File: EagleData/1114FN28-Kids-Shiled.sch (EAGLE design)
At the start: 18 parts

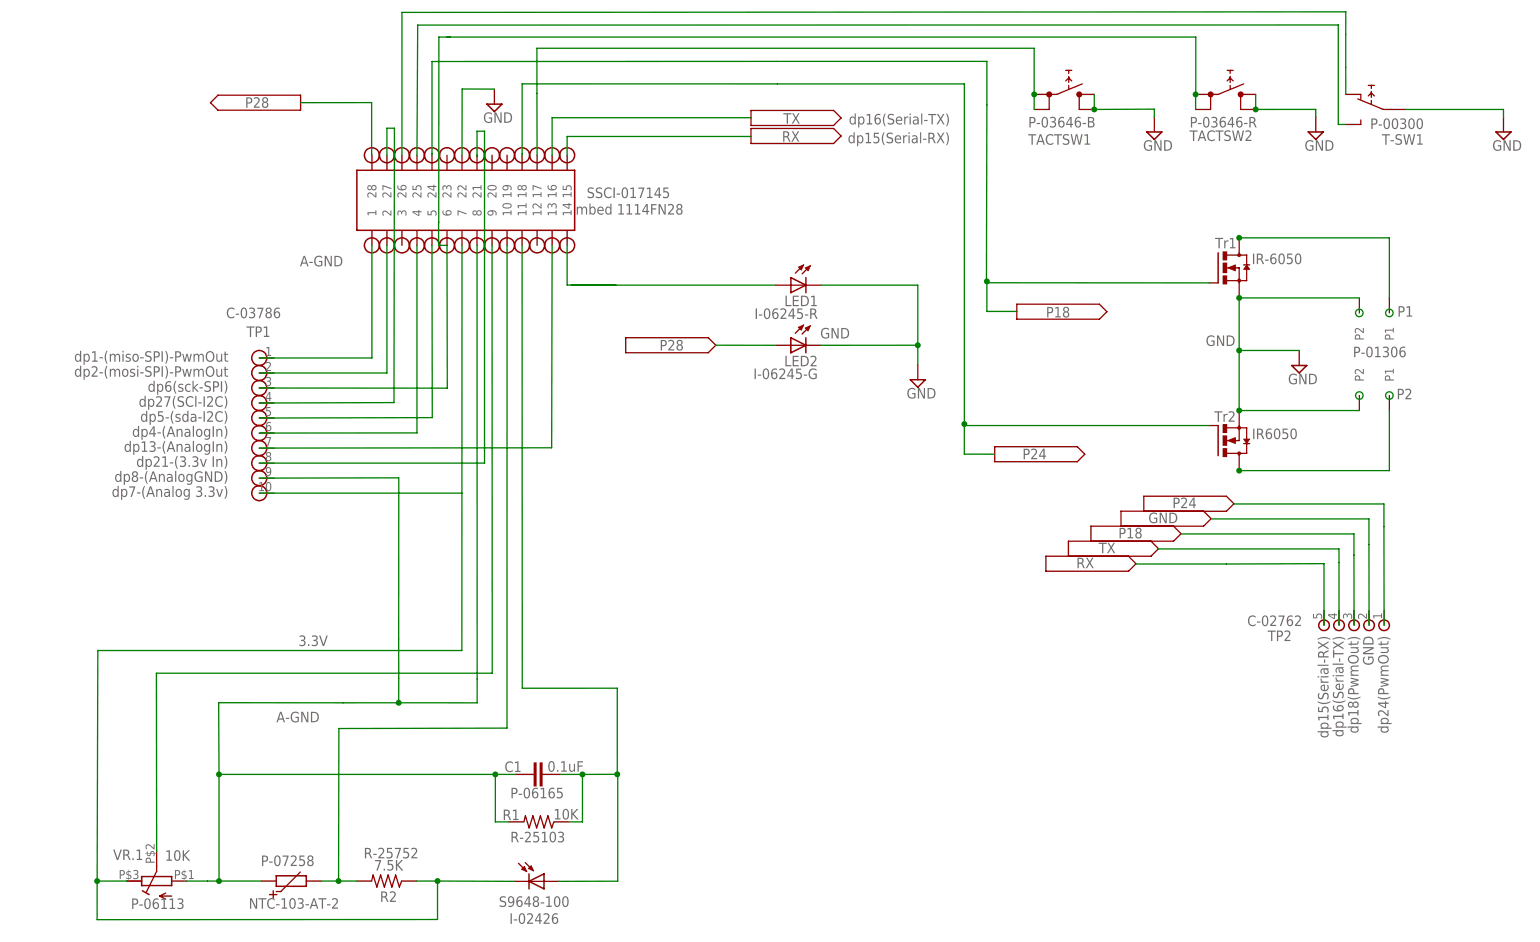
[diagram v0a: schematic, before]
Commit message: Change to FET part number.
I-6050 to I-6025 AKIZUKI part number.
IRLU3410PBF
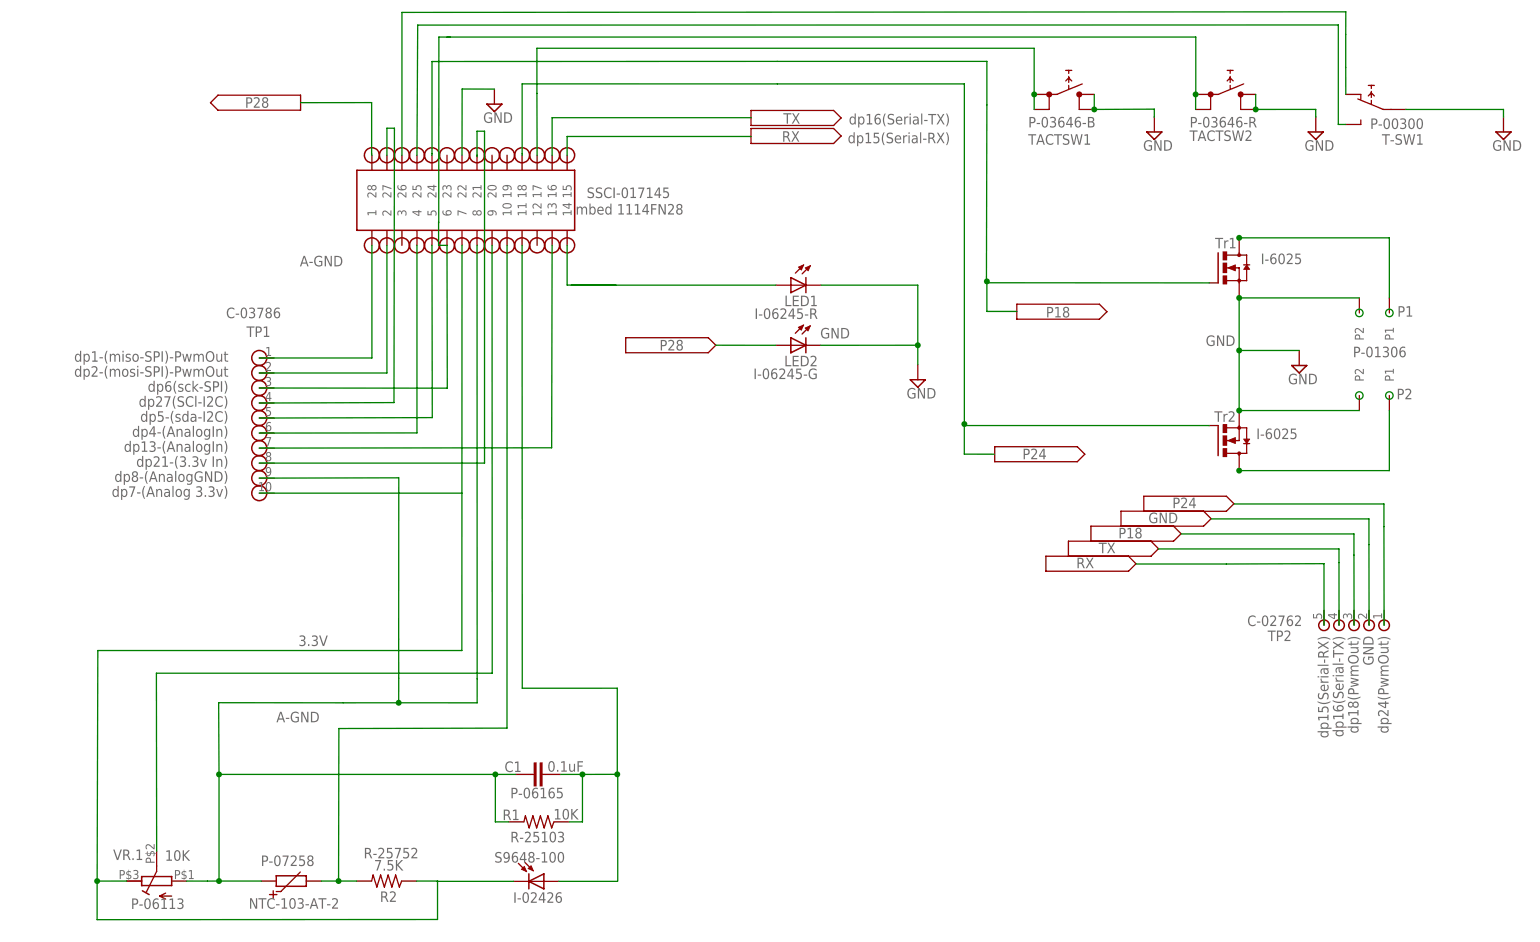
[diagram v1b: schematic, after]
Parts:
- U$2: device Aruduino-Kids-Shiled:S9648-100 -> 1114FN28-Kids-Shiled:S9648-100
- U$4: value IR-6050 -> I-6025
- U$5: value IR6050 -> I-6025
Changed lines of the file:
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@@
 <setting verticaltext="up"/>
 </settings>
-<grid distance="50" unitdist="mil" unit="mil" style="lines" multiple="1" display="yes" altdistance="5" altunitdist="mil" altunit="mil"/>
+<grid distance="5" unitdist="mil" unit="mil" style="lines" multiple="1" display="no" altdistance="5" altunitdist="mil" altunit="mil"/>
 <layers>
 <layer number="1" name="Top" color="4" fill="1" visible="no" active="no"/>
@@
 <part name="TB2" library="Aruduino-Kids-Shiled" deviceset="TB112-2-2-U-1" device="" value="P-01306"/>
 <part name="VR.1" library="Aruduino-Kids-Shiled" deviceset="TSR-3386K" device="" value="10K"/>
-<part name="U$4" library="Aruduino-Kids-Shiled" deviceset="ＩＲＦＵ１２０Ｎ" device="" value="IR-6050"/>
-<part name="U$5" library="Aruduino-Kids-Shiled" deviceset="ＩＲＦＵ１２０Ｎ" device="" value="IR6050"/>
+<part name="U$4" library="Aruduino-Kids-Shiled" deviceset="ＩＲＦＵ１２０Ｎ" device="" value="I-6025"/>
+<part name="U$5" library="Aruduino-Kids-Shiled" deviceset="ＩＲＦＵ１２０Ｎ" device="" value="I-6025"/>
 <part name="U$1" library="Aruduino-Kids-Shiled" deviceset="FH-1X14" device=""/>
-<part name="U$2" library="Aruduino-Kids-Shiled" deviceset="S9648-100" device=""/>
 <part name="C1" library="Aruduino-Kids-Shiled" deviceset="C-RPEF" device="" value="0.1uF"/>
 <part name="R1" library="Aruduino-Kids-Shiled" deviceset="R" device="" value="10K"/>
@@
 <part name="SUPPLY16" library="supply2" deviceset="V&lt;--" device="" value=""/>
 <part name="SUPPLY17" library="supply2" deviceset="V&lt;--" device="" value=""/>
+<part name="U$2" library="1114FN28-Kids-Shiled" deviceset="S9648-100" device=""/>
 </parts>
 <sheets>
@@
 <text x="-46.9646" y="-58.9788" size="1.778" layer="95" rot="R180" align="bottom-right">P-06165</text>
 <text x="-62.4586" y="-69.1388" size="1.778" layer="95" rot="MR180" align="bottom-right">R-25752</text>
-<text x="-47.117" y="-80.2132" size="1.778" layer="95" rot="R180" align="bottom-right">I-02426</text>
+<text x="-46.482" y="-76.6572" size="1.778" layer="95" rot="R180" align="bottom-right">I-02426</text>
 <text x="-85.725" y="20.447" size="1.778" layer="95" align="bottom-right">C-03786</text>
 <text x="-34.036" y="42.545" size="1.778" layer="95" rot="R180" align="bottom-right">SSCI-017145</text>
@@
 </instance>
 <instance part="U$1" gate="G$1" x="-53.848" y="40.386" rot="R90"/>
-<instance part="U$2" gate="G$1" x="-42.5196" y="-74.803" smashed="yes" rot="R180">
-<attribute name="VALUE" x="-36.9316" y="-77.343" size="1.778" layer="96" rot="R180"/>
-</instance>
 <instance part="C1" gate="G$1" x="-42.2402" y="-56.7182" smashed="yes" rot="R90">
 <attribute name="NAME" x="-45.0088" y="-54.5338" size="1.778" layer="95" rot="R180"/>
@@
 <instance part="SUPPLY16" gate="G$1" x="-6.239034375" y="54.3105375" rot="R180"/>
 <instance part="SUPPLY17" gate="G$1" x="-6.239034375" y="51.2625375" rot="R180"/>
+<instance part="U$2" gate="G$1" x="-42.545" y="-74.803" smashed="yes" rot="R180">
+<attribute name="VALUE" x="-49.657" y="-71.628" size="1.778" layer="96"/>
+</instance>
 </instances>
 <busses>
@@
 <wire x1="-116.834921875" y1="-81.285078125" x2="-59.2582" y2="-81.2546" width="0.1524" layer="91"/>
 <wire x1="-59.2582" y1="-81.2546" x2="-59.2582" y2="-74.7522" width="0.1524" layer="91"/>
-<wire x1="-59.2582" y1="-74.7522" x2="-46.3296" y2="-74.803" width="0.1524" layer="91"/>
-<pinref part="U$2" gate="G$1" pin="C"/>
 <junction x="-116.8298375" y="-74.757278125"/>
 <pinref part="R2" gate="G$1" pin="1"/>
 <label x="-77.8002" y="-33.2232" size="1.778" layer="95" rot="R180"/>
-<junction x="-59.2582" y="-74.7522"/>
 </segment>
 <segment>
 <pinref part="U$8" gate="G$1" pin="10"/>
 <wire x1="-89.408" y1="-9.144" x2="-55.118" y2="-9.144" width="0.254" layer="91"/>
+</segment>
+<segment>
+<pinref part="U$2" gate="G$1" pin="C"/>
+<wire x1="-46.355" y1="-74.803" x2="-59.309" y2="-74.803" width="0.254" layer="91"/>
 </segment>
 </net>
@@
 <wire x1="-34.7472" y1="-64.7446" x2="-34.7472" y2="-56.7182" width="0.1524" layer="91"/>
 <wire x1="-34.7472" y1="-56.7182" x2="-28.857959375" y2="-56.70115" width="0.1524" layer="91"/>
-<wire x1="-38.7096" y1="-74.803" x2="-28.7782" y2="-74.7776" width="0.1524" layer="91"/>
 <wire x1="-28.7782" y1="-74.7776" x2="-28.7782" y2="-56.7182" width="0.1524" layer="91"/>
 <wire x1="-28.7782" y1="-56.7182" x2="-28.857959375" y2="-56.70115" width="0.1524" layer="91"/>
-<pinref part="U$2" gate="G$1" pin="A"/>
 <wire x1="-44.958" y1="32.766" x2="-44.92679375" y2="-42.1423375" width="0.1524" layer="91"/>
 <wire x1="-44.92679375" y1="-42.1423375" x2="-28.8544" y2="-42.1386" width="0.1524" layer="91"/>
@@
 <junction x="-34.7472" y="-56.7182"/>
 </segment>
-</net>
+<segment>
+<pinref part="U$2" gate="G$1" pin="A"/>
+<wire x1="-38.735" y1="-74.803" x2="-28.829" y2="-74.803" width="0.254" layer="91"/>
+</segment>
+</net>
